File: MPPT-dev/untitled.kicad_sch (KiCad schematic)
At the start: 25 parts, among them Q1 PMOS, U2 LT8611EUDD-PBF, U3 AD5245BRJZ10-R2

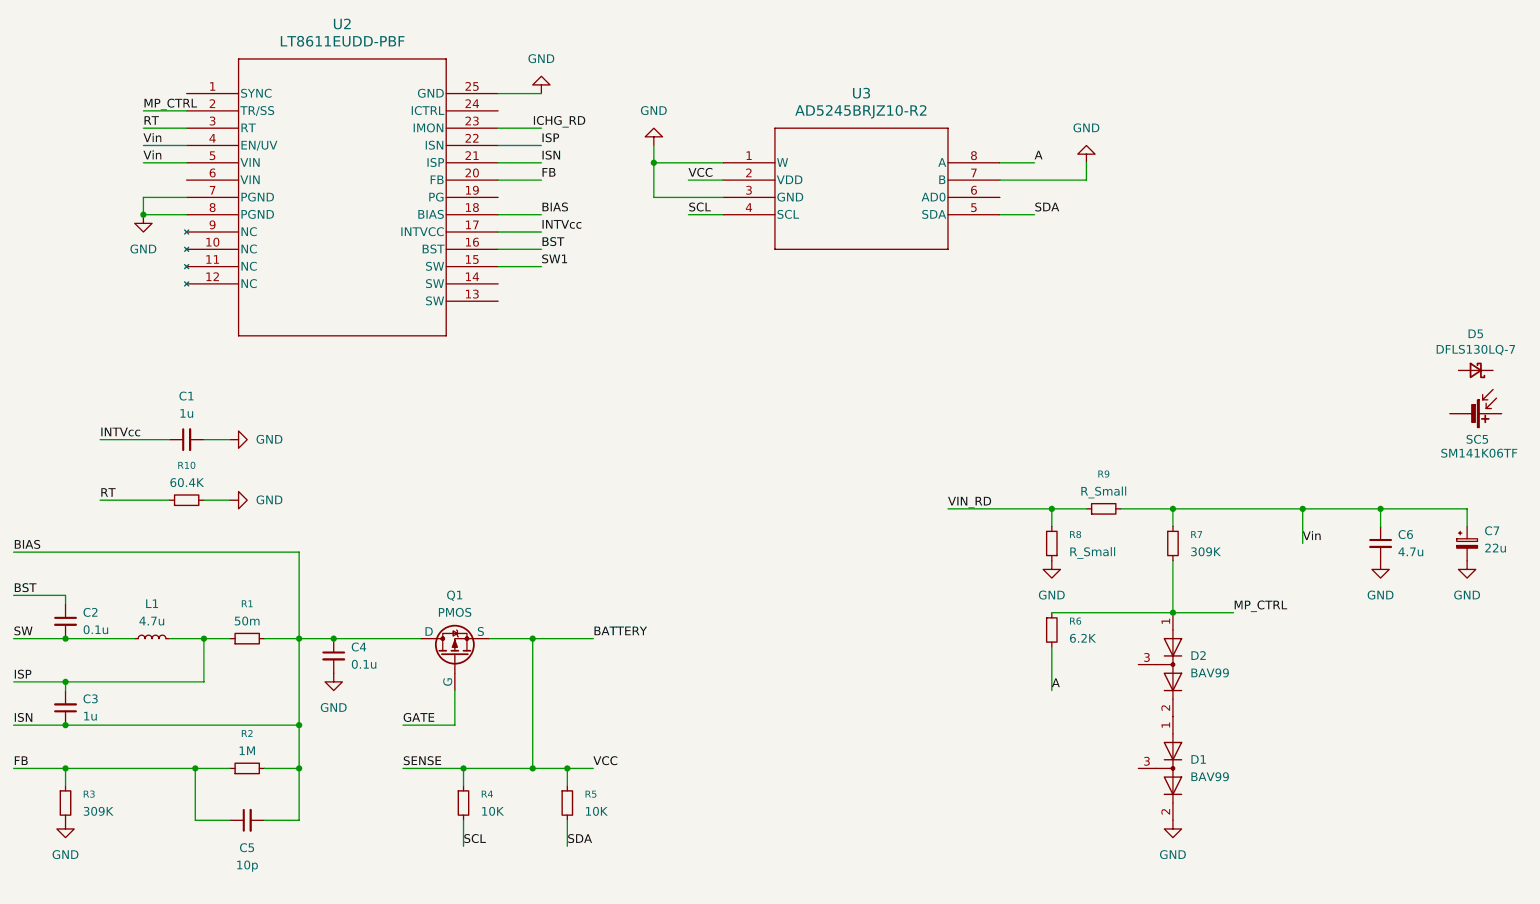
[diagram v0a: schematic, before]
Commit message: usb connector
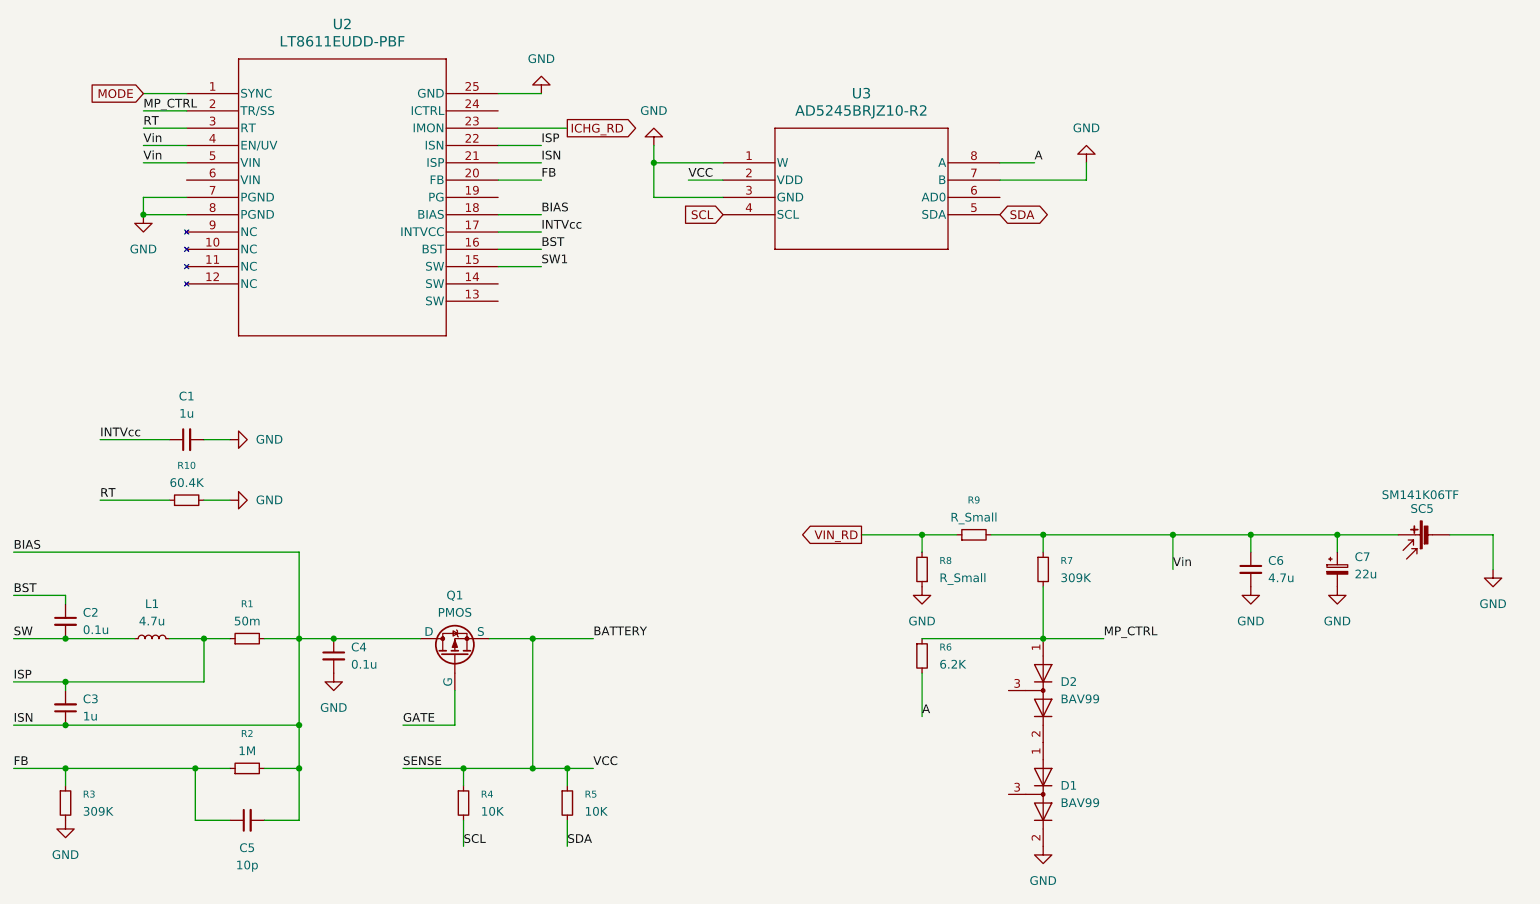
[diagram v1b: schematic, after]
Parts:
- removed D5: DFLS130LQ-7, Diode_SMD:D_PowerDI-123, symbol Device:D_Schottky_Small
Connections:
- net GND: now also SC5.2 (-)
- net Vin: now also SC5.1 (+)
- net MODE: now reaches U2.1 (SYNC)
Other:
- moved on the sheet: C6, C7, D1, D2, R6, R7, R8, R9, SC5
